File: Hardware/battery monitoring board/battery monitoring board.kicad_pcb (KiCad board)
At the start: 4 copper layers, 142 x 53.3 mm, 71 parts, among them J1 Conn_01x02, J10 9V Conn_01x02, J2 Conn_01x02, J3 S5B-XH-A, J4 Conn_01x02, J5 Conn_01x02, J6 Conn_01x02, J7 Conn_01x02, J8 Conn_01x02, J9 S5B-XH-A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

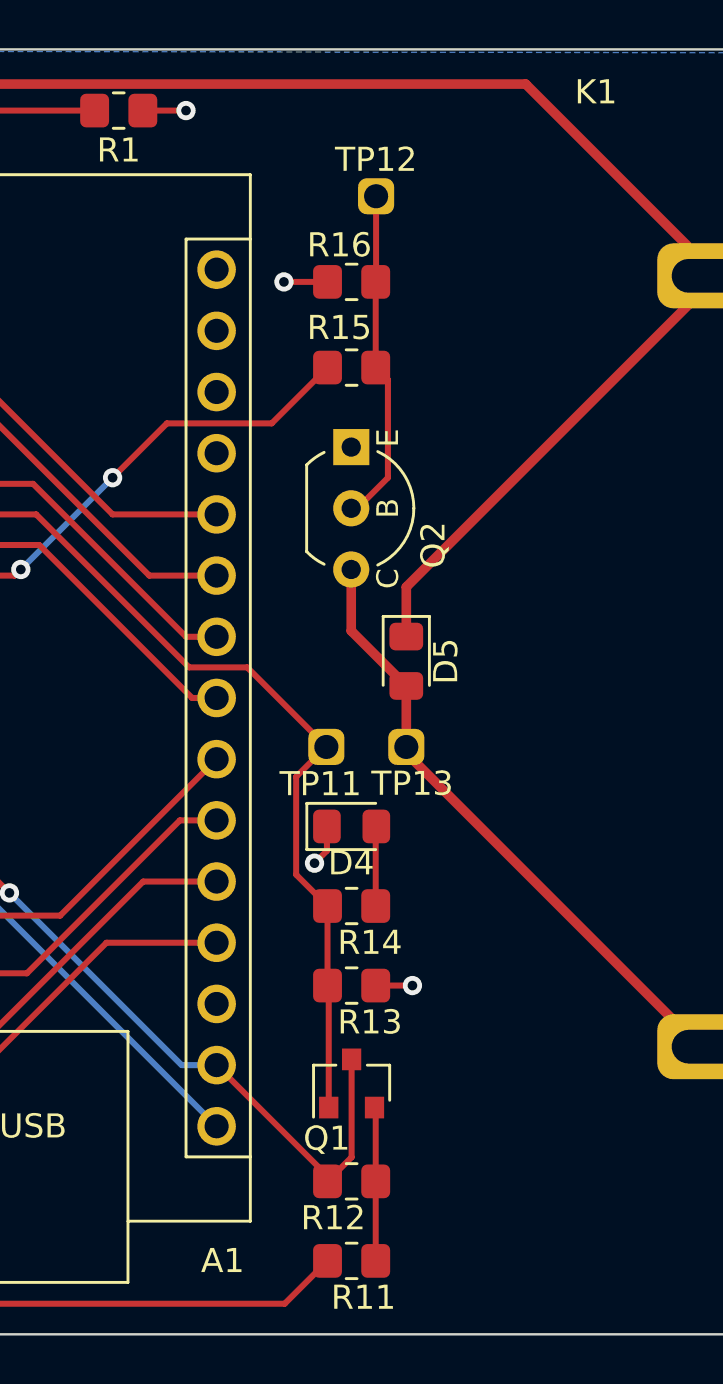
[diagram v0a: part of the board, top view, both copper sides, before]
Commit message: changed pnp footprint
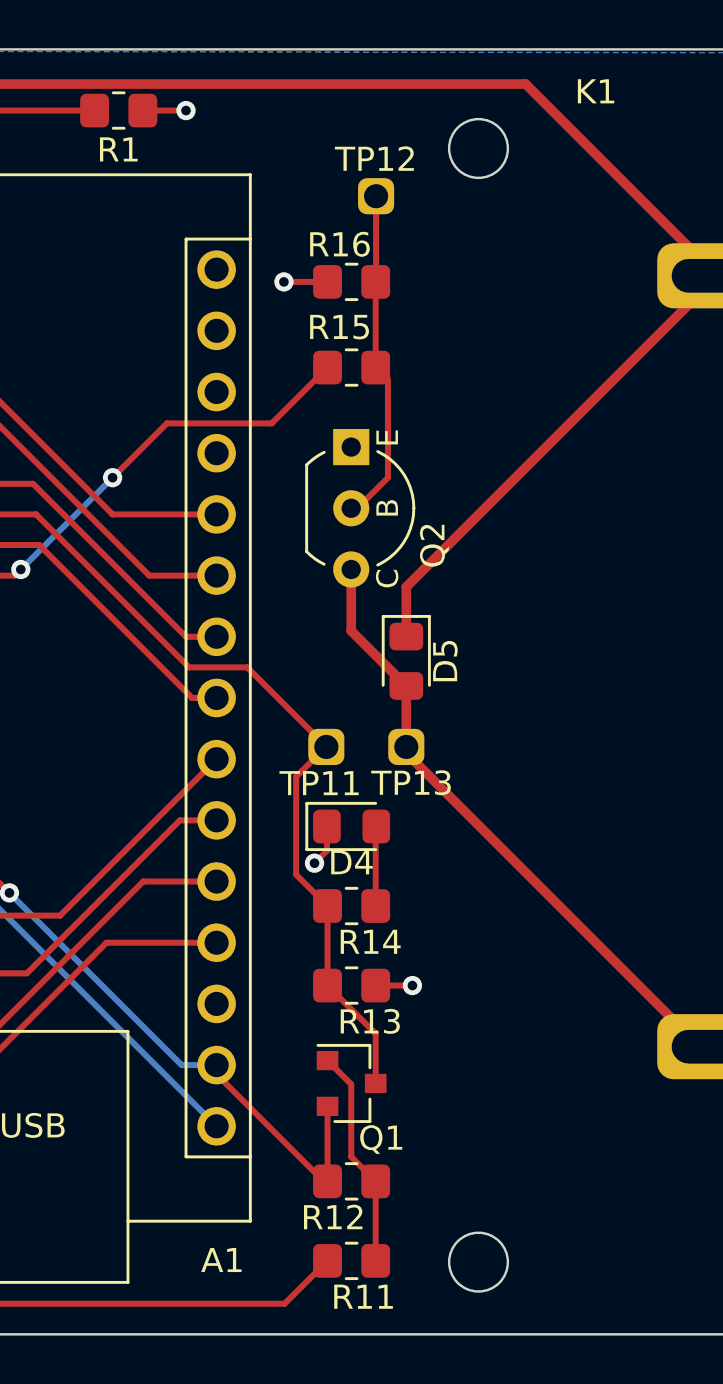
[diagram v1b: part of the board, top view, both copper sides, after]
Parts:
- turned Q1 to 0 degrees
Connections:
- Q1 pad 1: /leak sensor/LEAK_SIGNAL -> Net-(Q1-B)
- Q1 pad 2: Net-(Q1-B) -> +3V3
- Q1 pad 3: +3V3 -> /leak sensor/LEAK_SIGNAL
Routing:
- net Net-(Q1-B): track 6.39 -> 9.14 mm
- net +3V3: track 76.4 -> 74.1 mm
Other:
- outline, holes or cut-outs redrawn
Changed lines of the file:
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@@
   )
   (footprint "PCM_4ms_Package_SOT:SOT-23" (layer "F.Cu")
-    (at 145.304 63.246 90)
+    (at 145.304 63.246)
     (descr "SOT-23, Standard")
     (tags "SOT-23")
@@
     (property "ki_keywords" "simulation")
     (attr smd)
-    (fp_text reference "Q1" (at -2.286 -1.032 180) (layer "F.SilkS")
+    (fp_text reference "Q1" (at 1.254 2.286 180) (layer "F.SilkS")
         (effects (font (size 1 1) (thickness 0.15)))
     )
-    (fp_text value "PNP" (at 0 2.5 90) (layer "F.Fab")
+    (fp_text value "PNP" (at 0 2.5) (layer "F.Fab")
         (effects (font (size 1 1) (thickness 0.15)))
     )
-    (fp_text user "${REFERENCE}" (at 0 0) (layer "F.Fab")
+    (fp_text user "${REFERENCE}" (at 0 0 90) (layer "F.Fab")
         (effects (font (size 0.5 0.5) (thickness 0.075)))
     )
@@
     (fp_line (start 0.7 -1.52) (end 0.7 1.52)
       (stroke (width 0.1) (type solid)) (layer "F.Fab"))
-    (pad "1" smd rect (at -1 -0.95 90) (size 0.9 0.8) (layers "F.Cu" "F.Paste" "F.Mask")
-      (net 5 "/leak sensor/LEAK_SIGNAL") (pinfunction "C") (pintype "open_collector"))
-    (pad "2" smd rect (at -1 0.95 90) (size 0.9 0.8) (layers "F.Cu" "F.Paste" "F.Mask")
-      (net 49 "Net-(Q1-B)") (pinfunction "B") (pintype "input"))
-    (pad "3" smd rect (at 1 0 90) (size 0.9 0.8) (layers "F.Cu" "F.Paste" "F.Mask")
-      (net 17 "+3V3") (pinfunction "E") (pintype "open_emitter"))
+    (pad "1" smd rect (at -1 -0.95) (size 0.9 0.8) (layers "F.Cu" "F.Paste" "F.Mask")
+      (net 49 "Net-(Q1-B)") (pinfunction "C") (pintype "open_collector"))
+    (pad "2" smd rect (at -1 0.95) (size 0.9 0.8) (layers "F.Cu" "F.Paste" "F.Mask")
+      (net 17 "+3V3") (pinfunction "B") (pintype "input"))
+    (pad "3" smd rect (at 1 0) (size 0.9 0.8) (layers "F.Cu" "F.Paste" "F.Mask")
+      (net 5 "/leak sensor/LEAK_SIGNAL") (pinfunction "E") (pintype "open_emitter"))
     (model "${KISYS3DMOD}/Package_TO_SOT_SMD.3dshapes/SOT-23.wrl"
       (offset (xyz 0 0 0))
@@
   (gr_arc (start 224.536 71.628) (mid 223.940841 73.064841) (end 222.504 73.66)
     (stroke (width 0.1) (type default)) (layer "Edge.Cuts"))
+  (gr_circle (center 150.5712 70.6628) (end 151.7904 70.6628)
+    (stroke (width 0.1) (type default)) (fill none) (layer "Edge.Cuts"))
   (gr_circle (center 85.09 71.12) (end 86.3092 71.12)
     (stroke (width 0.1) (type default)) (fill none) (layer "Edge.Cuts"))
+  (gr_circle (center 150.5712 24.4348) (end 151.7904 24.4348)
+    (stroke (width 0.1) (type default)) (fill none) (layer "Edge.Cuts"))
   (gr_circle (center 222.0468 22.86) (end 223.266 22.86)
     (stroke (width 0.1) (type default)) (fill none) (layer "Edge.Cuts"))
@@
   (via (at 220.726 50.546) (size 1.2) (drill 0.4) (layers "F.Cu" "B.Cu") (net 4))
   (via (at 218.694 35.052) (size 1.2) (drill 0.4) (layers "F.Cu" "B.Cu") (net 4))
-  (segment (start 144.354 64.246) (end 144.354 59.486) (width 0.25) (layer "F.Cu") (net 5))
+  (segment (start 144.304 59.182) (end 146.304 61.182) (width 0.25) (layer "F.Cu") (net 5))
   (segment (start 144.304 55.88) (end 143.002 54.578) (width 0.25) (layer "F.Cu") (net 5))
   (segment (start 132.208396 39.624) (end 124.46 39.624) (width 0.25) (layer "F.Cu") (net 5))
@@
   (segment (start 143.002 54.578) (end 143.002 50.514) (width 0.25) (layer "F.Cu") (net 5))
   (segment (start 144.256 49.26) (end 140.97 45.974) (width 0.25) (layer "F.Cu") (net 5))
+  (segment (start 146.304 61.182) (end 146.304 63.246) (width 0.25) (layer "F.Cu") (net 5))
   (segment (start 144.304 59.182) (end 144.304 55.88) (width 0.25) (layer "F.Cu") (net 5))
   (segment (start 144.272 49.276) (end 144.256 49.26) (width 0.25) (layer "F.Cu") (net 5))
   (segment (start 140.97 45.974) (end 138.558396 45.974) (width 0.25) (layer "F.Cu") (net 5))
   (segment (start 144.025 56.109) (end 144.05 56.134) (width 0.25) (layer "F.Cu") (net 5))
-  (segment (start 144.354 59.232) (end 144.304 59.182) (width 0.25) (layer "F.Cu") (net 5))
   (segment (start 135.382 38.1) (end 137.636 35.846) (width 0.25) (layer "F.Cu") (net 6))
   (segment (start 137.636 35.846) (end 141.986 35.846) (width 0.25) (layer "F.Cu") (net 6))
@@
   (via (at 127.254 52.578) (size 0.8) (drill 0.4) (layers "F.Cu" "B.Cu") (net 16))
   (segment (start 127.254 52.578) (end 139.7 65.024) (width 0.25) (layer "B.Cu") (net 16))
-  (segment (start 144.304 67.31) (end 144.304 67.088) (width 0.25) (layer "F.Cu") (net 17))
   (segment (start 115.062 50.514) (end 115.094 50.546) (width 0.25) (layer "F.Cu") (net 17))
   (segment (start 115.094 50.546) (end 119.1685 50.546) (width 0.25) (layer "F.Cu") (net 17))
   (segment (start 115.062 43.434) (end 118.9145 43.434) (width 0.25) (layer "F.Cu") (net 17))
+  (segment (start 144.145 67.31) (end 139.7 62.865) (width 0.25) (layer "F.Cu") (net 17))
+  (segment (start 144.304 67.31) (end 144.145 67.31) (width 0.25) (layer "F.Cu") (net 17))
   (segment (start 122.2165 53.594) (end 120.4385 51.816) (width 0.25) (layer "F.Cu") (net 17))
-  (segment (start 145.304 66.31) (end 145.304 62.246) (width 0.25) (layer "F.Cu") (net 17))
   (segment (start 105.602 51.562) (end 103.697 49.657) (width 0.25) (layer "F.Cu") (net 17))
-  (segment (start 144.304 67.088) (end 139.7 62.484) (width 0.25) (layer "F.Cu") (net 17))
   (segment (start 125.222 45.974) (end 124.146122 45.974) (width 0.25) (layer "F.Cu") (net 17))
   (segment (start 118.9145 43.434) (end 120.4385 41.91) (width 0.25) (layer "F.Cu") (net 17))
+  (segment (start 144.304 67.31) (end 144.304 64.196) (width 0.25) (layer "F.Cu") (net 17))
   (segment (start 126.238 46.99) (end 125.222 45.974) (width 0.25) (layer "F.Cu") (net 17))
   (segment (start 119.1685 50.546) (end 120.4385 51.816) (width 0.25) (layer "F.Cu") (net 17))
@@
   (segment (start 114.014 51.562) (end 105.602 51.562) (width 0.25) (layer "F.Cu") (net 17))
   (segment (start 131.09975 55.33625) (end 126.238 50.4745) (width 0.25) (layer "F.Cu") (net 17))
+  (segment (start 139.7 62.865) (end 139.7 62.484) (width 0.25) (layer "F.Cu") (net 17))
   (segment (start 120.4385 42.266378) (end 120.4385 41.91) (width 0.25) (layer "F.Cu") (net 17))
   (segment (start 124.146122 45.974) (end 120.4385 42.266378) (width 0.25) (layer "F.Cu") (net 17))
-  (segment (start 144.304 67.31) (end 145.304 66.31) (width 0.25) (layer "F.Cu") (net 17))
   (segment (start 115.062 50.514) (end 114.014 51.562) (width 0.25) (layer "F.Cu") (net 17))
   (via (at 131.09975 55.33625) (size 0.8) (drill 0.4) (layers "F.Cu" "B.Cu") (net 17))
@@
   (segment (start 106.696 34.56) (end 105.776 35.48) (width 0.25) (layer "F.Cu") (net 48))
   (segment (start 111.252 34.56) (end 106.696 34.56) (width 0.25) (layer "F.Cu") (net 48))
-  (segment (start 146.304 67.31) (end 146.304 64.296) (width 0.25) (layer "F.Cu") (net 49))
+  (segment (start 146.304 67.31) (end 145.288 66.294) (width 0.25) (layer "F.Cu") (net 49))
+  (segment (start 145.288 63.28) (end 144.304 62.296) (width 0.25) (layer "F.Cu") (net 49))
+  (segment (start 145.288 66.294) (end 145.288 63.28) (width 0.25) (layer "F.Cu") (net 49))
   (segment (start 146.304 70.612) (end 146.304 67.31) (width 0.25) (layer "F.Cu") (net 49))
-  (segment (start 146.304 64.296) (end 146.254 64.246) (width 0.25) (layer "F.Cu") (net 49))
   (segment (start 146.304 29.972) (end 146.304 33.528) (width 0.25) (layer "F.Cu") (net 50))
   (segment (start 146.32 29.956) (end 146.304 29.972) (width 0.25) (layer "F.Cu") (net 50))
